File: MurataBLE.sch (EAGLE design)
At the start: 54 parts, among them CON1 47589-0001, IC1 I-5448, IC2 LPC11U35_QFN33, IC3 NC7SZ00, IC4 AT25DN512C, IC5 AT25XE011, P1 NC, P2 NC, P3 NC, P4 NC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

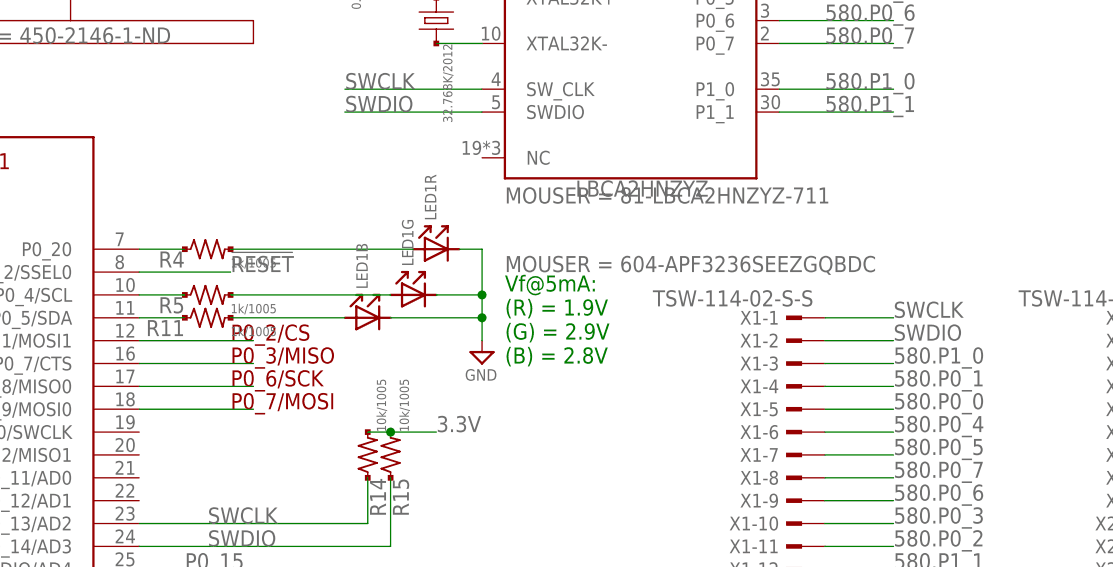
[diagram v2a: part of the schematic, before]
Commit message: [ USB ] fix OpenDrain problem
P0_4 and 5 are used for I2C; has limitation of open drain
change polarity of LED1 to pull current from 3.3V line
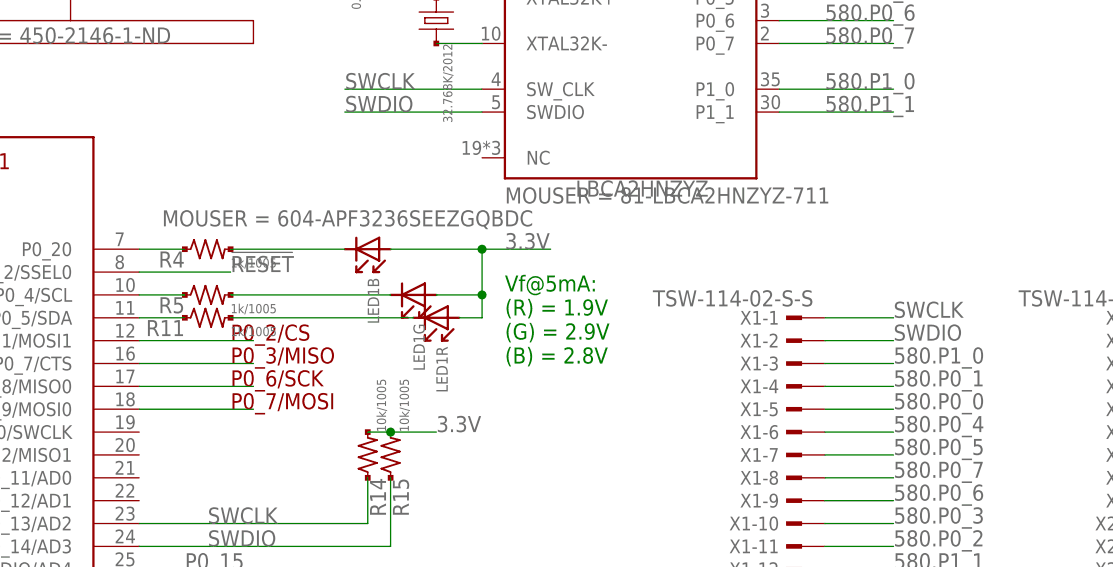
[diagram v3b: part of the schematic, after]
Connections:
- net 3.3V: now also LED1B.A, LED1G.A, LED1R.A
- net GND: no longer LED1B.K, LED1G.K, LED1R.K
- net N$11: now also LED1R.K, R11.2; no longer LED1R.A, R4.2
- net N$12: now also LED1G.K; no longer LED1G.A
- net N$13: now also LED1B.K, R4.2; no longer LED1B.A, R11.2
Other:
- moved on the sheet: LED1B, LED1G, LED1R
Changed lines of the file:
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@@
 <part name="R5" library="mylib" deviceset="R_US_*" device="_1005" technology="1.0K" value="1k/1005"/>
 <part name="R11" library="mylib" deviceset="R_US_*" device="_1005" technology="1.0K" value="1k/1005"/>
-<part name="SUPPLY16" library="mylib" deviceset="GND" device=""/>
 <part name="LED1" library="mylib" deviceset="LED_3SEG" device=""/>
 <part name="X1" library="mylib" deviceset="TSW-114-02-S-S" device="" value="TSW-114-02-S-S">
@@
 <instance part="R5" gate="G$1" x="165.1" y="96.52"/>
 <instance part="R11" gate="G$1" x="165.1" y="93.98"/>
-<instance part="SUPPLY16" gate="GND" x="195.58" y="88.9"/>
-<instance part="LED1" gate="R" x="190.5" y="101.6" rot="R90"/>
-<instance part="LED1" gate="G" x="187.96" y="96.52" rot="R90">
-<attribute name="MOUSER" x="198.12" y="99.06" size="1.778" layer="96" display="both"/>
-</instance>
-<instance part="LED1" gate="B" x="182.88" y="93.98" rot="R90"/>
+<instance part="LED1" gate="R" x="190.5" y="93.98" rot="R270"/>
+<instance part="LED1" gate="G" x="187.96" y="96.52" rot="R270">
+<attribute name="MOUSER" x="160.02" y="104.14" size="1.778" layer="96" display="both"/>
+</instance>
+<instance part="LED1" gate="B" x="182.88" y="101.6" rot="R270"/>
 <instance part="X1" gate="-1" x="231.14" y="93.98" rot="MR0">
 <attribute name="NOT_COMPONENT" x="231.14" y="93.98" size="1.778" layer="96" rot="MR0" display="off"/>
@@
 </segment>
 <segment>
-<wire x1="193.04" y1="101.6" x2="195.58" y2="101.6" width="0.1524" layer="91"/>
-<wire x1="195.58" y1="101.6" x2="195.58" y2="96.52" width="0.1524" layer="91"/>
-<wire x1="195.58" y1="96.52" x2="195.58" y2="93.98" width="0.1524" layer="91"/>
-<wire x1="195.58" y1="93.98" x2="195.58" y2="91.44" width="0.1524" layer="91"/>
-<wire x1="185.42" y1="93.98" x2="195.58" y2="93.98" width="0.1524" layer="91"/>
-<junction x="195.58" y="93.98"/>
-<wire x1="190.5" y1="96.52" x2="195.58" y2="96.52" width="0.1524" layer="91"/>
-<junction x="195.58" y="96.52"/>
-<pinref part="SUPPLY16" gate="GND" pin="GND"/>
-<pinref part="LED1" gate="R" pin="K"/>
-<pinref part="LED1" gate="G" pin="K"/>
-<pinref part="LED1" gate="B" pin="K"/>
-</segment>
-<segment>
 <pinref part="IC4" gate="G$1" pin="GND"/>
 <pinref part="SUPPLY17" gate="GND" pin="GND"/>
@@
 <junction x="185.42" y="81.28"/>
 </segment>
+<segment>
+<wire x1="195.58" y1="101.6" x2="203.2" y2="101.6" width="0.1524" layer="91"/>
+<wire x1="195.58" y1="93.98" x2="195.58" y2="96.52" width="0.1524" layer="91"/>
+<pinref part="LED1" gate="G" pin="A"/>
+<wire x1="195.58" y1="96.52" x2="195.58" y2="101.6" width="0.1524" layer="91"/>
+<wire x1="190.5" y1="96.52" x2="195.58" y2="96.52" width="0.1524" layer="91"/>
+<junction x="195.58" y="96.52"/>
+<label x="198.12" y="101.6" size="1.778" layer="95"/>
+<pinref part="LED1" gate="R" pin="A"/>
+<wire x1="193.04" y1="93.98" x2="195.58" y2="93.98" width="0.1524" layer="91"/>
+<pinref part="LED1" gate="B" pin="A"/>
+<wire x1="185.42" y1="101.6" x2="195.58" y2="101.6" width="0.1524" layer="91"/>
+<junction x="195.58" y="101.6"/>
+</segment>
 </net>
 <net name="RESET" class="0">
@@
 </segment>
 </net>
-<net name="N$11" class="0">
-<segment>
-<pinref part="R4" gate="G$1" pin="2"/>
-<wire x1="167.64" y1="101.6" x2="187.96" y2="101.6" width="0.1524" layer="91"/>
-<pinref part="LED1" gate="R" pin="A"/>
-</segment>
-</net>
-<net name="N$12" class="0">
-<segment>
-<pinref part="R5" gate="G$1" pin="2"/>
-<wire x1="185.42" y1="96.52" x2="167.64" y2="96.52" width="0.1524" layer="91"/>
-<pinref part="LED1" gate="G" pin="A"/>
-</segment>
-</net>
-<net name="N$13" class="0">
-<segment>
-<pinref part="R11" gate="G$1" pin="2"/>
-<wire x1="167.64" y1="93.98" x2="180.34" y2="93.98" width="0.1524" layer="91"/>
-<pinref part="LED1" gate="B" pin="A"/>
-</segment>
-</net>
 <net name="580.P0_1" class="0">
 <segment>
@@
 </segment>
 </net>
+<net name="N$12" class="0">
+<segment>
+<pinref part="R5" gate="G$1" pin="2"/>
+<pinref part="LED1" gate="G" pin="K"/>
+<wire x1="167.64" y1="96.52" x2="185.42" y2="96.52" width="0.1524" layer="91"/>
+</segment>
+</net>
+<net name="N$11" class="0">
+<segment>
+<pinref part="R11" gate="G$1" pin="2"/>
+<pinref part="LED1" gate="R" pin="K"/>
+<wire x1="167.64" y1="93.98" x2="187.96" y2="93.98" width="0.1524" layer="91"/>
+</segment>
+</net>
+<net name="N$13" class="0">
+<segment>
+<pinref part="LED1" gate="B" pin="K"/>
+<pinref part="R4" gate="G$1" pin="2"/>
+<wire x1="180.34" y1="101.6" x2="167.64" y2="101.6" width="0.1524" layer="91"/>
+</segment>
+</net>

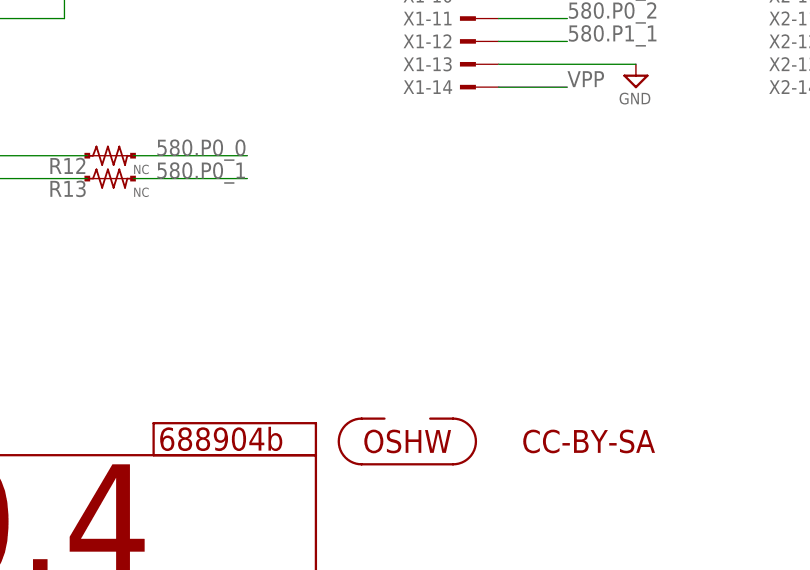
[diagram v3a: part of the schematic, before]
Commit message: [ USB ] add LED2, R16-18
UART TX/RX LEDs and blinky a LED combined to LED2
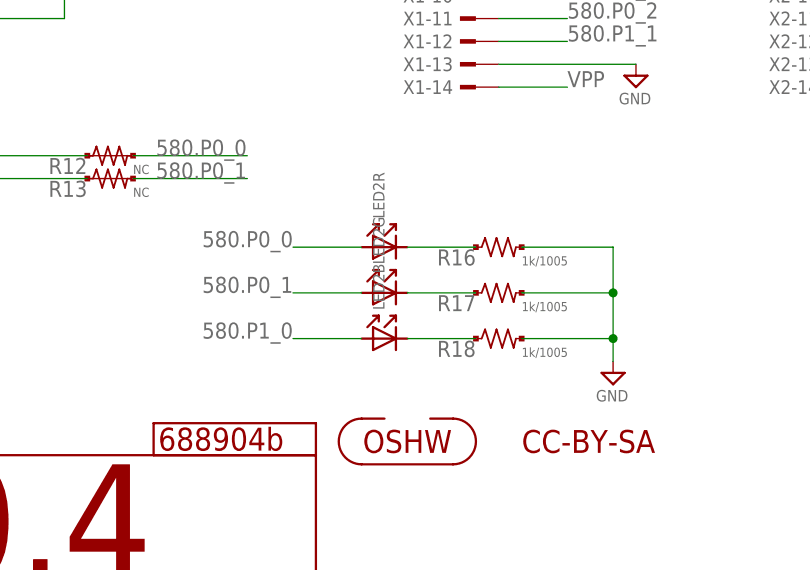
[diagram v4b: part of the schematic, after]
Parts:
- added LED2: LED_3SEG, mylib:LED_3SEG
- added R16, R17, R18: 1k/1005, mylib:R_US_1.0K_1005
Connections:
- new net N$14: LED2B.K, R18.1
- new net N$15: LED2G.K, R17.1
- new net N$16: LED2R.K, R16.1
- net 580.P0_0: now also LED2R.A
- net 580.P0_1: now also LED2G.A
- net 580.P1_0: now also LED2B.A
- net GND: now also R16.2, R17.2, R18.2
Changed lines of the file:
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@@
 <part name="R14" library="mylib" deviceset="R_US_*" device="_1005" technology="10K" value="10k/1005"/>
 <part name="R15" library="mylib" deviceset="R_US_*" device="_1005" technology="10K" value="10k/1005"/>
+<part name="LED2" library="mylib" deviceset="LED_3SEG" device=""/>
+<part name="R16" library="mylib" deviceset="R_US_*" device="_1005" technology="1.0K" value="1k/1005"/>
+<part name="R17" library="mylib" deviceset="R_US_*" device="_1005" technology="1.0K" value="1k/1005"/>
+<part name="R18" library="mylib" deviceset="R_US_*" device="_1005" technology="1.0K" value="1k/1005"/>
+<part name="SUPPLY7" library="mylib" deviceset="GND" device=""/>
 </parts>
 <sheets>
@@
 <instance part="R14" gate="G$1" x="182.88" y="78.74" rot="R90"/>
 <instance part="R15" gate="G$1" x="185.42" y="78.74" rot="R90"/>
+<instance part="LED2" gate="B" x="220.98" y="33.02" rot="R90"/>
+<instance part="LED2" gate="G" x="220.98" y="38.1" rot="R90"/>
+<instance part="LED2" gate="R" x="220.98" y="43.18" rot="R90"/>
+<instance part="R16" gate="G$1" x="233.68" y="43.18"/>
+<instance part="R17" gate="G$1" x="233.68" y="38.1"/>
+<instance part="R18" gate="G$1" x="233.68" y="33.02"/>
+<instance part="SUPPLY7" gate="GND" x="246.38" y="27.94"/>
 </instances>
 <busses>
@@
 <junction x="58.42" y="27.94"/>
 </segment>
+<segment>
+<pinref part="R16" gate="G$1" pin="2"/>
+<pinref part="SUPPLY7" gate="GND" pin="GND"/>
+<wire x1="236.22" y1="43.18" x2="246.38" y2="43.18" width="0.1524" layer="91"/>
+<wire x1="246.38" y1="43.18" x2="246.38" y2="38.1" width="0.1524" layer="91"/>
+<pinref part="R17" gate="G$1" pin="2"/>
+<wire x1="246.38" y1="38.1" x2="246.38" y2="33.02" width="0.1524" layer="91"/>
+<wire x1="246.38" y1="33.02" x2="246.38" y2="30.48" width="0.1524" layer="91"/>
+<wire x1="236.22" y1="38.1" x2="246.38" y2="38.1" width="0.1524" layer="91"/>
+<junction x="246.38" y="38.1"/>
+<pinref part="R18" gate="G$1" pin="2"/>
+<wire x1="236.22" y1="33.02" x2="246.38" y2="33.02" width="0.1524" layer="91"/>
+<junction x="246.38" y="33.02"/>
+</segment>
 </net>
 <net name="N$2" class="0">
@@
 <label x="241.3" y="88.9" size="1.778" layer="95"/>
 </segment>
+<segment>
+<wire x1="210.82" y1="33.02" x2="218.44" y2="33.02" width="0.1524" layer="91"/>
+<pinref part="LED2" gate="B" pin="A"/>
+<label x="210.82" y="33.02" size="1.778" layer="95" rot="MR0"/>
+</segment>
 </net>
 <net name="580.P1_1" class="0">
@@
 <label x="195.58" y="53.34" size="1.778" layer="95"/>
 </segment>
+<segment>
+<wire x1="210.82" y1="43.18" x2="218.44" y2="43.18" width="0.1524" layer="91"/>
+<pinref part="LED2" gate="R" pin="A"/>
+<label x="210.82" y="43.18" size="1.778" layer="95" rot="MR0"/>
+</segment>
 </net>
 <net name="N$4" class="0">
@@
 <pinref part="X1" gate="-4" pin="1"/>
 </segment>
+<segment>
+<wire x1="210.82" y1="38.1" x2="218.44" y2="38.1" width="0.1524" layer="91"/>
+<pinref part="LED2" gate="G" pin="A"/>
+<label x="210.82" y="38.1" size="1.778" layer="95" rot="MR0"/>
+</segment>
 </net>
 <net name="P1_15" class="0">
@@
 </segment>
 </net>
+<net name="N$14" class="0">
+<segment>
+<pinref part="LED2" gate="B" pin="K"/>
+<pinref part="R18" gate="G$1" pin="1"/>
+<wire x1="223.52" y1="33.02" x2="231.14" y2="33.02" width="0.1524" layer="91"/>
+</segment>
+</net>
+<net name="N$15" class="0">
+<segment>
+<pinref part="LED2" gate="G" pin="K"/>
+<pinref part="R17" gate="G$1" pin="1"/>
+<wire x1="223.52" y1="38.1" x2="231.14" y2="38.1" width="0.1524" layer="91"/>
+</segment>
+</net>
+<net name="N$16" class="0">
+<segment>
+<pinref part="R16" gate="G$1" pin="1"/>
+<pinref part="LED2" gate="R" pin="K"/>
+<wire x1="231.14" y1="43.18" x2="223.52" y2="43.18" width="0.1524" layer="91"/>
+</segment>
+</net>

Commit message: [ USB ] IC1 replace and necessary moves
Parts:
- IC1: value I-5448 -> (none); device mylib:LDO5_3.3_SOT23 -> mylib:LDO4_3.3_DRJ
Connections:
- removed net N$5: IC2.!RESET!, IC3.1B, R9.2
- new net NSRST: IC2.P0_2/SSEL0, IC3.1A, IC3.1B, R1.2
- net !RESET!: now also IC2.!RESET!, R9.2; no longer IC2.P0_2/SSEL0, IC3.1A, R1.2
- net VUSB: no longer IC1.E
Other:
- moved on the sheet: C1, C10, C11, C12, C13, C2, C3, C4, C5, C6, C7, C8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

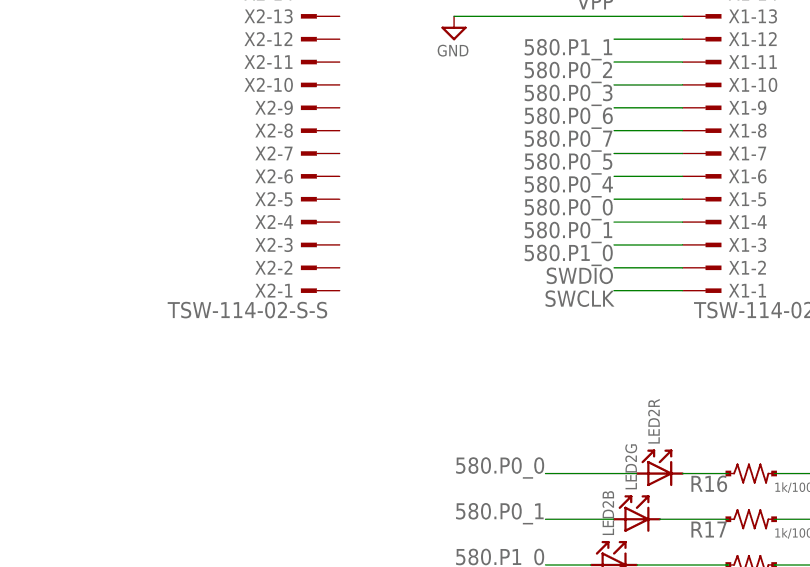
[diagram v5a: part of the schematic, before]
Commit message: [ USB ] add 3.3V pin; silk; move R4/5/11
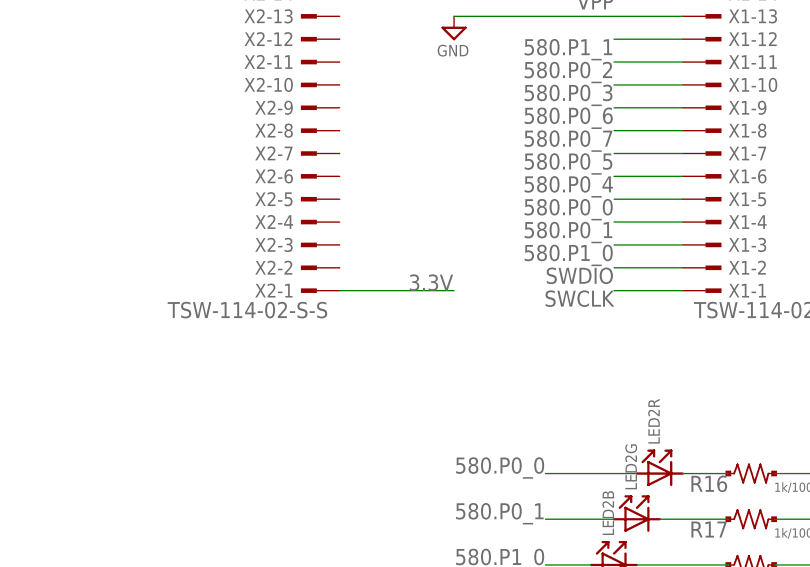
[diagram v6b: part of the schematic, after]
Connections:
- net 3.3V: now also X2-1.1
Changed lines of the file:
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@@
 <label x="111.76" y="71.12" size="1.778" layer="95"/>
+</segment>
+<segment>
+<wire x1="317.5" y1="66.04" x2="330.2" y2="66.04" width="0.1524" layer="91"/>
+<pinref part="X2" gate="-1" pin="1"/>
+<label x="325.12" y="66.04" size="1.778" layer="95"/>
 </segment>
 </net>
